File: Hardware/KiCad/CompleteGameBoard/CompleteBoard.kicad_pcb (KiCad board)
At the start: 4 copper layers, 181.6 x 111.8 mm, 26 parts

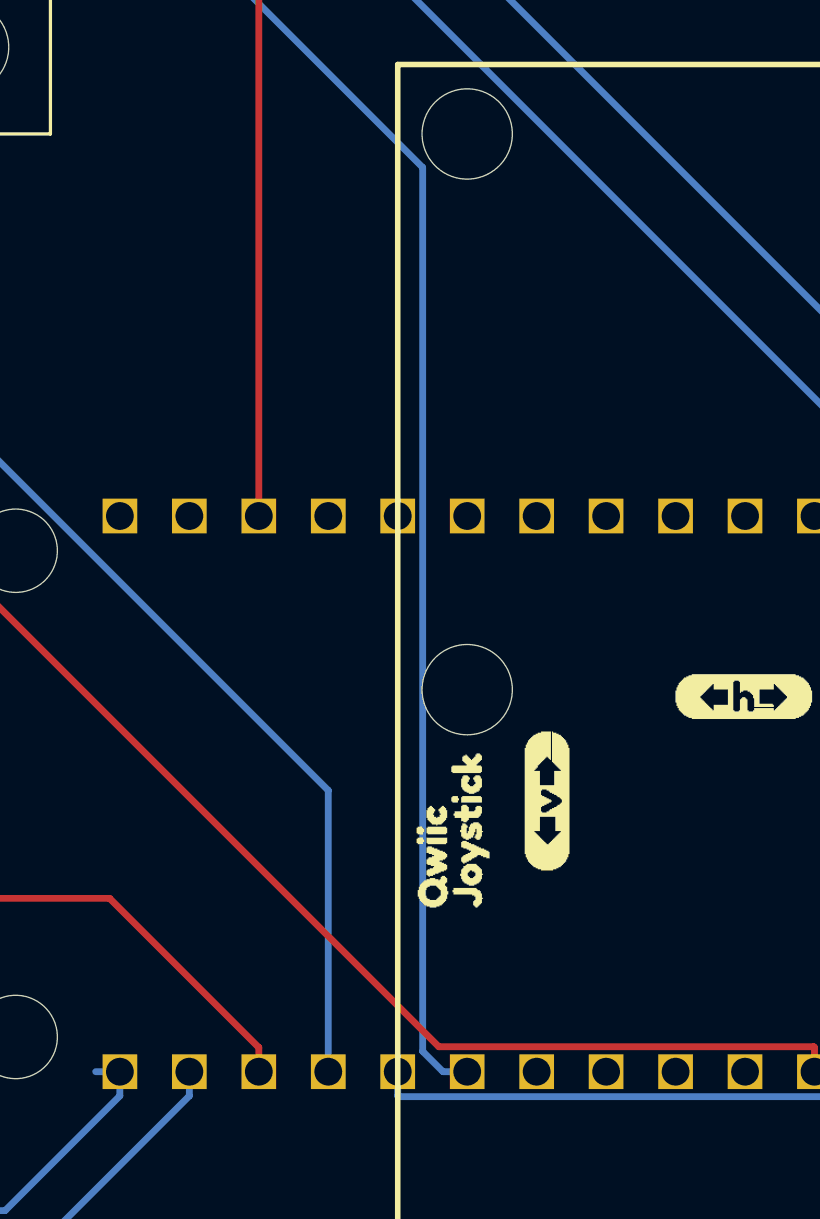
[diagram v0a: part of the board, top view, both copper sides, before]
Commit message: Fixed traces for the 'complete board' for issue #20
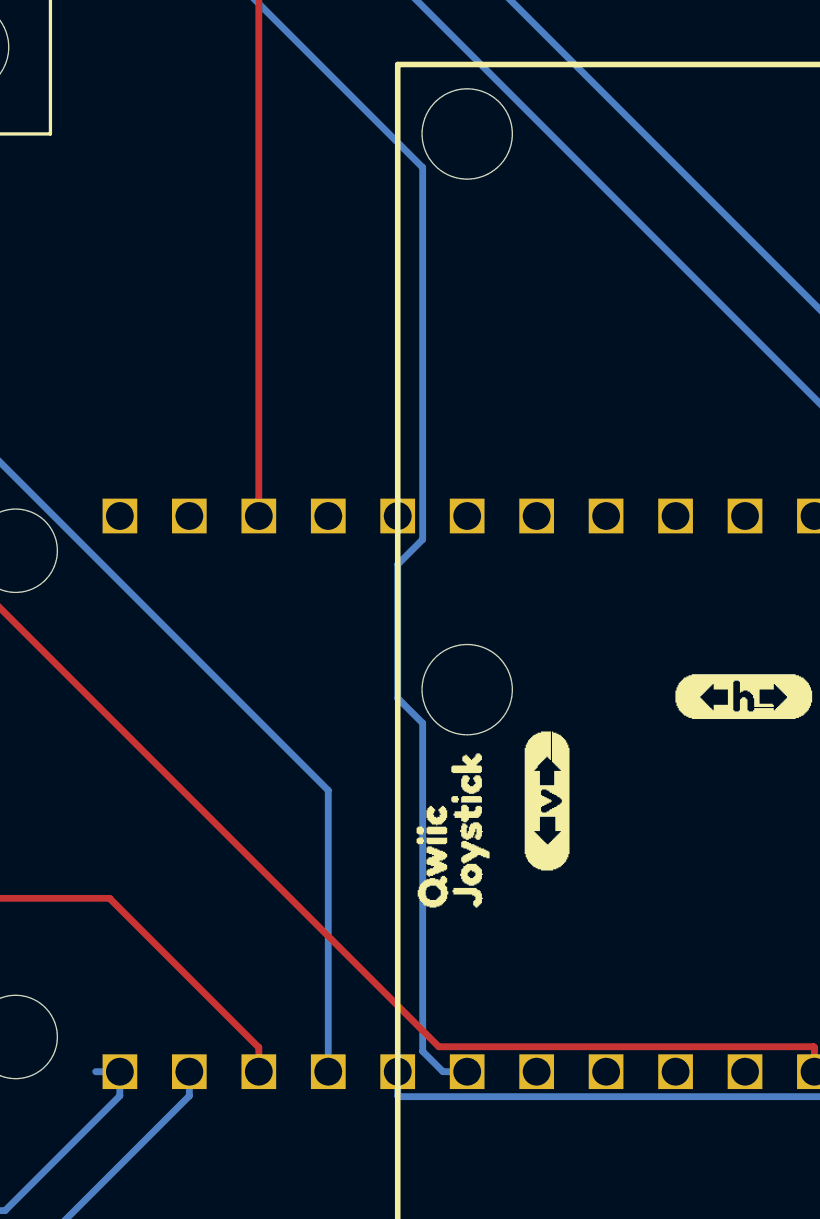
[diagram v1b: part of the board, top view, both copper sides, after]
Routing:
- net GND: track 394.7 -> 404.4 mm
- net SCLK: track 56.9 -> 57.6 mm
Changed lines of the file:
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@@
     (thickness 1.6)
     (drawings 683)
-    (tracks 150)
+    (tracks 157)
     (zones 0)
     (modules 26)
@@
   (segment (start 170.18 85.09) (end 176.53 91.44) (width 0.25) (layer In1.Cu) (net 1))
   (segment (start 204.47 65.48) (end 188.52 49.53) (width 0.25) (layer In1.Cu) (net 1))
-  (segment (start 193.810678 118.11) (end 204.47 118.11) (width 0.25) (layer In1.Cu) (net 1))
-  (segment (start 183.237599 107.536921) (end 193.810678 118.11) (width 0.25) (layer In1.Cu) (net 1))
   (segment (start 183.237599 103.227599) (end 183.237599 107.536921) (width 0.25) (layer In1.Cu) (net 1))
   (segment (start 176.53 96.52) (end 183.237599 103.227599) (width 0.25) (layer In1.Cu) (net 1))
@@
   (segment (start 204.47 118.11) (end 204.47 65.48) (width 0.25) (layer In1.Cu) (net 1))
   (segment (start 204.47 127) (end 204.47 118.11) (width 0.25) (layer In1.Cu) (net 1))
+  (segment (start 194.31 118.11) (end 185.42 118.11) (width 0.25) (layer In1.Cu) (net 1))
+  (segment (start 193.810678 118.11) (end 194.31 118.11) (width 0.25) (layer In1.Cu) (net 1))
+  (segment (start 194.31 118.11) (end 204.47 118.11) (width 0.25) (layer In1.Cu) (net 1))
+  (segment (start 183.237599 115.927599) (end 183.237599 103.227599) (width 0.25) (layer In1.Cu) (net 1))
+  (segment (start 185.42 118.11) (end 183.237599 115.927599) (width 0.25) (layer In1.Cu) (net 1))
   (segment (start 53.570501 121.829499) (end 54.65 120.75) (width 0.25) (layer In1.Cu) (net 2))
   (segment (start 53.293099 122.106901) (end 53.570501 121.829499) (width 0.25) (layer In1.Cu) (net 2))
@@
   (segment (start 170.18 72.39) (end 172.846074 72.39) (width 0.25) (layer Bottom) (net 29))
   (segment (start 185.062401 93.936435) (end 176.53 85.404034) (width 0.25) (layer Bottom) (net 30))
-  (segment (start 185.062401 126.257401) (end 185.062401 93.936435) (width 0.25) (layer Bottom) (net 30))
   (segment (start 185.805 127) (end 185.062401 126.257401) (width 0.25) (layer Bottom) (net 30))
   (segment (start 186.69 127) (end 185.805 127) (width 0.25) (layer Bottom) (net 30))
@@
   (segment (start 176.53 83.82) (end 171.119799 78.409799) (width 0.25) (layer Top) (net 30))
   (segment (start 176.53 85.09) (end 176.53 83.82) (width 0.25) (layer Top) (net 30))
+  (segment (start 185.062401 107.536921) (end 185.062401 93.936435) (width 0.25) (layer Bottom) (net 30))
+  (segment (start 184.15 113.344034) (end 184.15 108.449322) (width 0.25) (layer Bottom) (net 30))
+  (segment (start 185.062401 114.256435) (end 184.15 113.344034) (width 0.25) (layer Bottom) (net 30))
+  (segment (start 184.15 108.449322) (end 185.062401 107.536921) (width 0.25) (layer Bottom) (net 30))
+  (segment (start 185.062401 126.257401) (end 185.062401 114.256435) (width 0.25) (layer Bottom) (net 30))
   (segment (start 154.9 115.61) (end 154.94 115.57) (width 0.25) (layer In1.Cu) (net 31))
   (segment (start 154.94 121.98) (end 154.9 122.02) (width 0.25) (layer In1.Cu) (net 31))
